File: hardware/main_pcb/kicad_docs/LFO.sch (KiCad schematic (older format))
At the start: 12 parts, among them J10 SWD_header, U8 STM32L031F4Px, U9 MCP4821

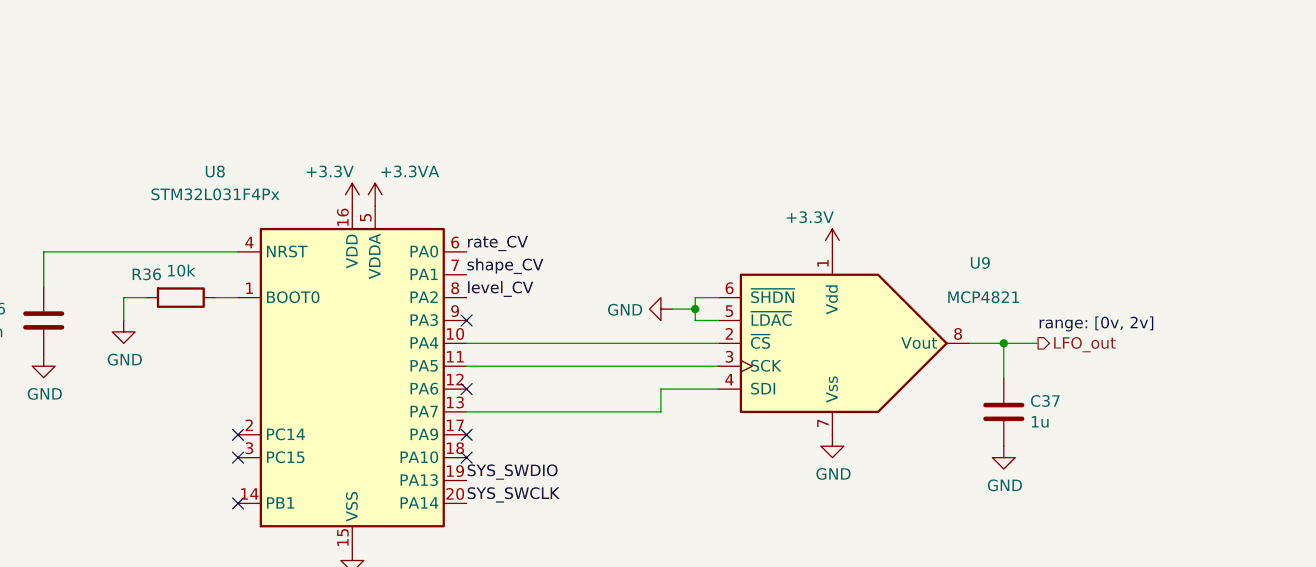
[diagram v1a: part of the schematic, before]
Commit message: center envelope follower around +1v, tidy up
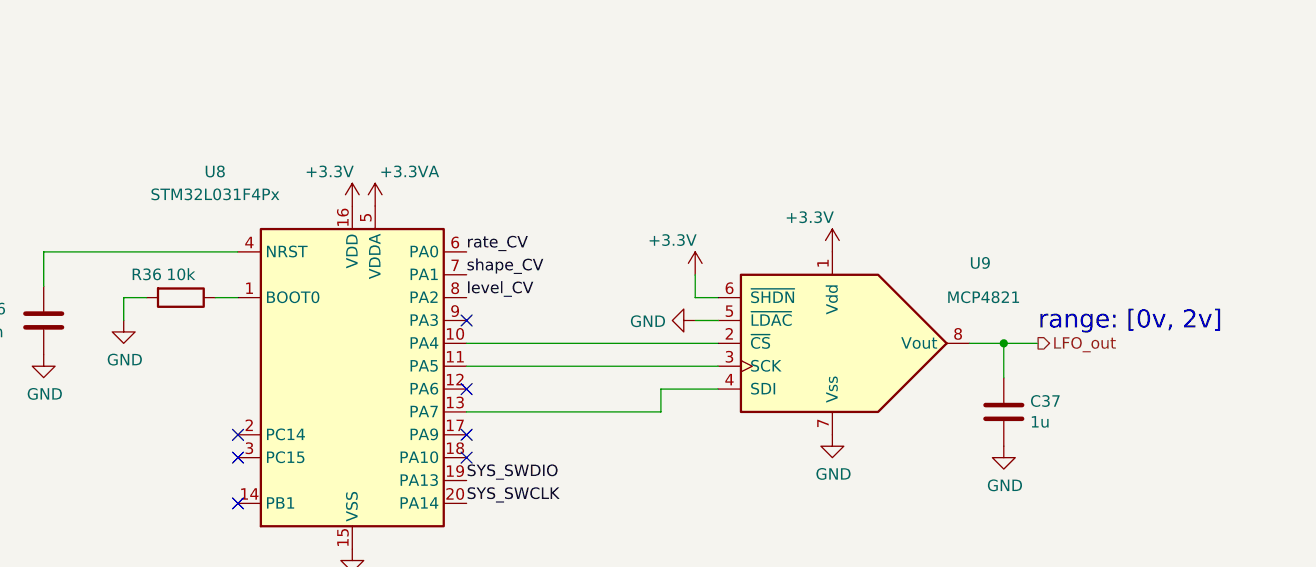
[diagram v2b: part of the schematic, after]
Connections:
- net +3V3: now also U9.6 (~SHDN)
- net GND: no longer U9.6 (~SHDN)
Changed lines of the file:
@@
 Sheet 5 8
 Title "Whooshy Sound Filter Pedal"
-Date "2021-06-29"
-Rev "0"
+Date "2021-08-05"
+Rev "0.1"
 Comp ""
 Comment1 "creativecommons.org/licenses/by/4.0/"
@@
 P 4800 3350
 F 0 "R36" V 4700 3200 50  0000 C CNN
-F 1 "10k" V 4684 3350 50  0000 C CNN
+F 1 "10k" V 4700 3350 50  0000 C CNN
 F 2 "Resistor_SMD:R_0805_2012Metric" V 4730 3350 50  0001 C CNN
 F 3 "~" H 4800 3350 50  0001 C CNN
@@
 Wire Wire Line
 	6900 3850 6050 3850
-$Comp
-L power:GND #PWR065
-U 1 1 60D2D0BF
-P 6950 3400
-F 0 "#PWR065" H 6950 3150 50  0001 C CNN
-F 1 "GND" V 6955 3272 50  0000 R CNN
-F 2 "" H 6950 3400 50  0001 C CNN
-F 3 "" H 6950 3400 50  0001 C CNN
-	1    6950 3400
-	0    1    1    0
-$EndComp
 Wire Wire Line
 	7150 3350 7050 3350
 Wire Wire Line
-	7050 3350 7050 3400
-Wire Wire Line
 	7050 3450 7150 3450
-Wire Wire Line
-	7050 3400 6950 3400
-Connection ~ 7050 3400
-Wire Wire Line
-	7050 3400 7050 3450
 $Comp
 L Device:R_POT RV8
@@
 	8400 3550 8250 3550
 NoConn ~ 6050 3750
-Text Notes 8550 3500 0    50   ~ 0
+Text Notes 8550 3500 0    79   ~ 0
 range: [0v, 2v]
+$Comp
+L power:GND #PWR065
+U 1 1 60D2D0BF
+P 7050 3450
+F 0 "#PWR065" H 7050 3200 50  0001 C CNN
+F 1 "GND" V 7055 3322 50  0000 R CNN
+F 2 "" H 7050 3450 50  0001 C CNN
+F 3 "" H 7050 3450 50  0001 C CNN
+	1    7050 3450
+	0    1    1    0
+$EndComp
+$Comp
+L power:+3.3V #PWR0104
+U 1 1 60F980E6
+P 7050 3250
+F 0 "#PWR0104" H 7050 3100 50  0001 C CNN
+F 1 "+3.3V" H 6950 3400 50  0000 C CNN
+F 2 "" H 7050 3250 50  0001 C CNN
+F 3 "" H 7050 3250 50  0001 C CNN
+	1    7050 3250
+	1    0    0    -1
+$EndComp
+Wire Wire Line
+	7050 3250 7050 3350
 $EndSCHEMATC
